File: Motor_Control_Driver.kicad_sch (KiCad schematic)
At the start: 10 parts, among them IC1002 DRV8214RTER

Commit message: Added footprints, images, almost finished all èages except for the MCU
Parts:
- R1002: renamed from R621; footprint (none) -> Resistor_SMD:R_0402_1005Metric; Manufacturer (none) -> KOA Speer; Manufacturer Part Number (none) -> RK73H1ETTP3300F; Supplier (none) -> Mouser Electronics; Supplier Part Number (none) -> 660-RK73H1ETTP3300F
- renumbered C622 to C1001, C620 to C1002, C624 to C1003, IC1002 to IC1001, LED502 to LED1001, R619 to R1001, R623 to R1003, TP602 to TP1001, TP604 to TP1002
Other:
- note added: "WQFN-16 3x3 mm"

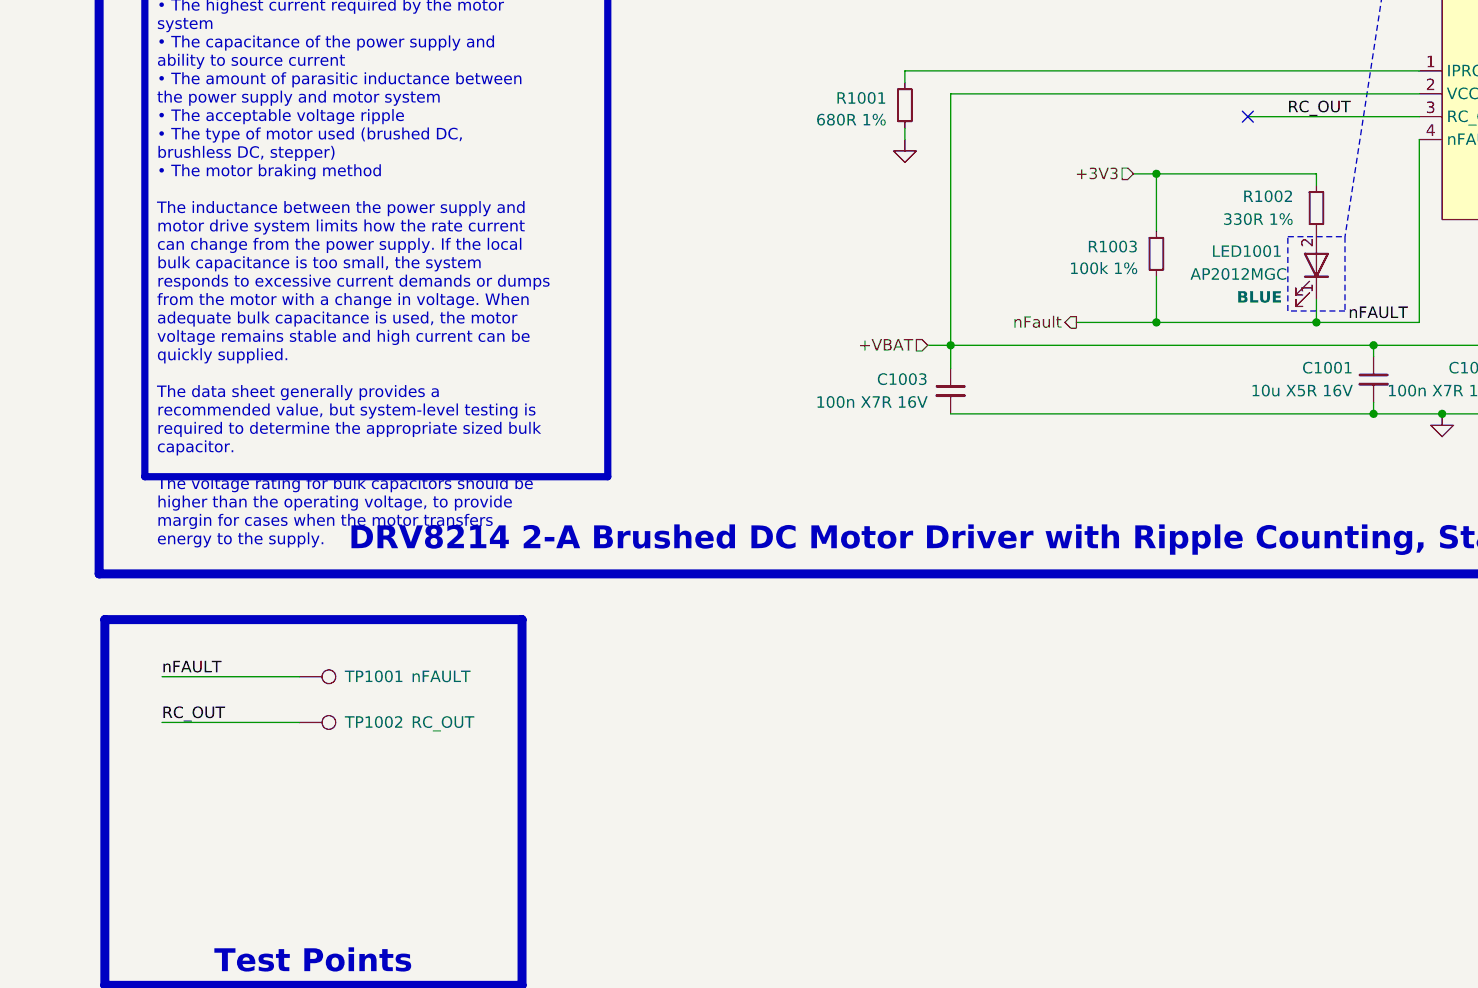
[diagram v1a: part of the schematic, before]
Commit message: Added RGB LED, added motor connectors, added test points, imported all 3D models
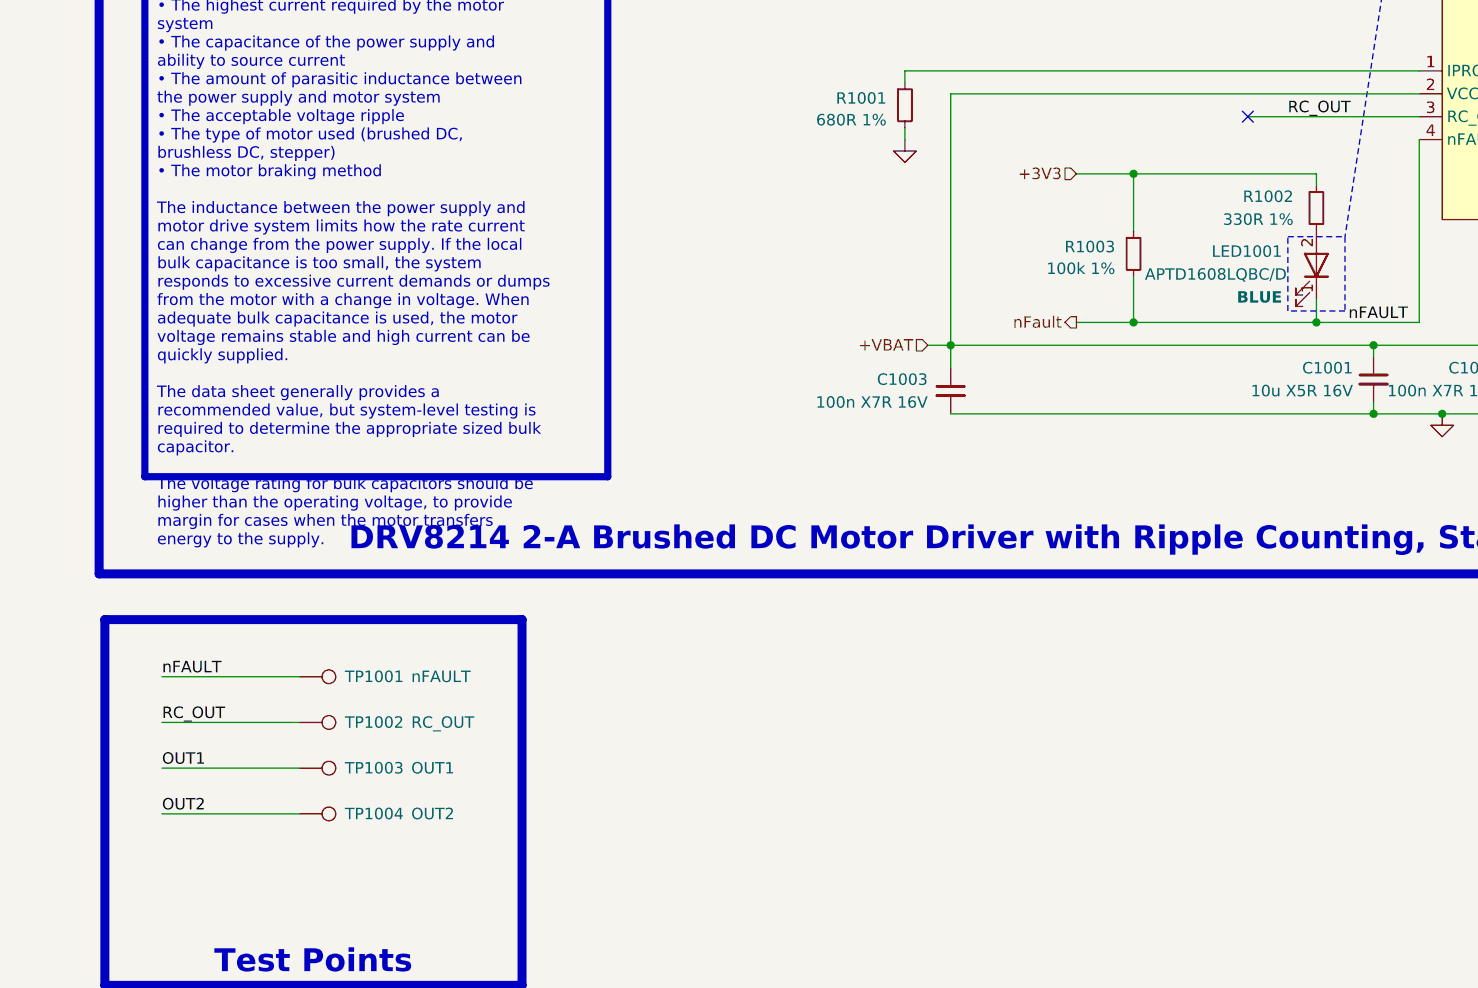
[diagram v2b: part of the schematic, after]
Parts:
- added TP1003: OUT1, 0_Plume:TestPoint_Pad_D0.5mm_Back, symbol Connector:TestPoint
- added TP1004: OUT2, 0_Plume:TestPoint_Pad_D0.5mm_Back, symbol Connector:TestPoint
- IC1001: footprint Package_DFN_QFN:WQFN-16-1EP_3x3mm_P0.5mm_EP1.68x1.68mm_ThermalVias -> 0_Plume:WQFN-16-1EP_3x3mm_P0.5mm_EP1.68x1.68mm_ThermalVias; Manufacturer (none) -> Texas Instruments; Manufacturer Part Number (none) -> DRV8214RTER; Supplier (none) -> Mouser Electronics; Supplier Part Number (none) -> 595-DRV8214RTER
- LED1001: footprint Charge_Manager_FP:KingBright_LED_0805 -> 0_Plume:KingBright_LED_0603; Manufacturer Part Number AP2012MGC -> APTD1608LQBC/D; Supplier Part Number 604-AP2012MGC -> 604-APTD1608LQBCD
- TP1001, TP1002: footprint 0_Zenith:TestPoint_Pad_D0.5mm_Front -> 0_Plume:TestPoint_Pad_D0.5mm_Back
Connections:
- net OUT1: now also TP1003.1
- net OUT2: now also TP1004.1
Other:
- moved on the sheet: R1003

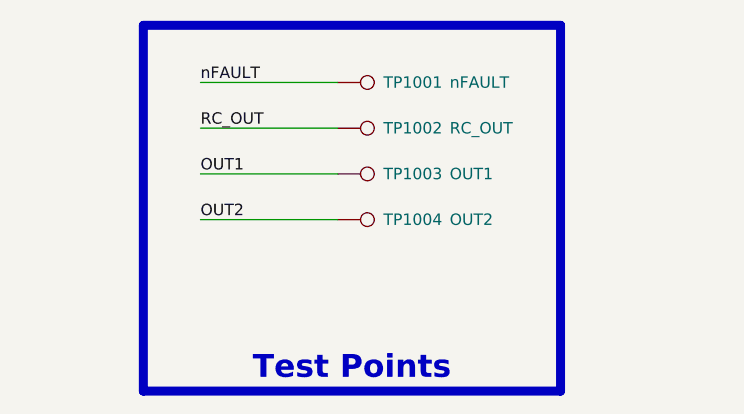
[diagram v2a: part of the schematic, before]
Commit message: Finished schematic, imported all footprints, all 3D models and created STM32 project, now need to proofread shematic before layout
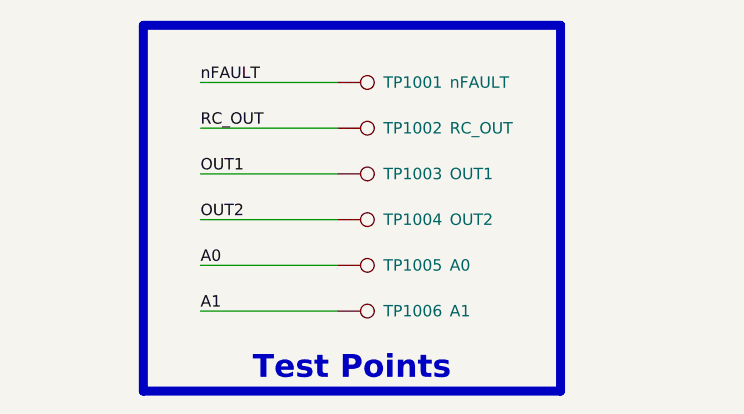
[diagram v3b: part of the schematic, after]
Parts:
- added TP1005: A0, 0_Plume:TestPoint_Pad_D0.5mm_Back, symbol Connector:TestPoint
- added TP1006: A1, 0_Plume:TestPoint_Pad_D0.5mm_Back, symbol Connector:TestPoint
- R1001: Manufacturer Panasonic -> (none); Manufacturer Part Number ERJ-2RKF1003X -> (none); Supplier Part Number 667-ERJ-2RKF1003X -> (none)
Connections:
- net A0: now also TP1005.1
- net A1: now also TP1006.1

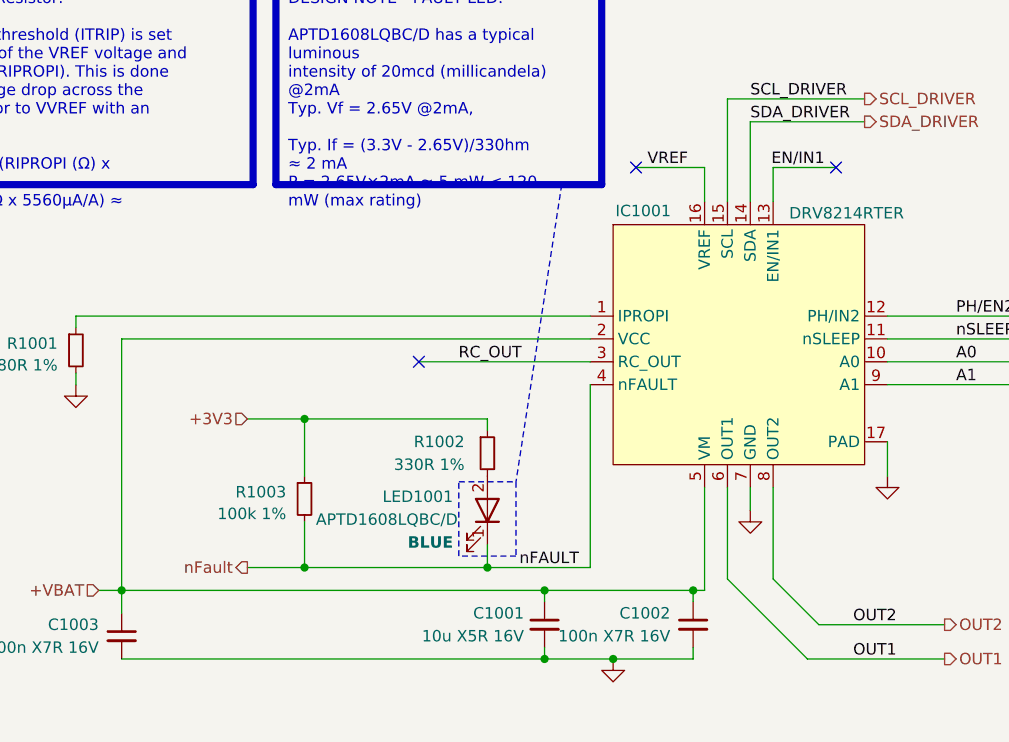
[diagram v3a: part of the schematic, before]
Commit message: Reviewed shematic, cleaned all DRC errors, chosed stackup, started layout
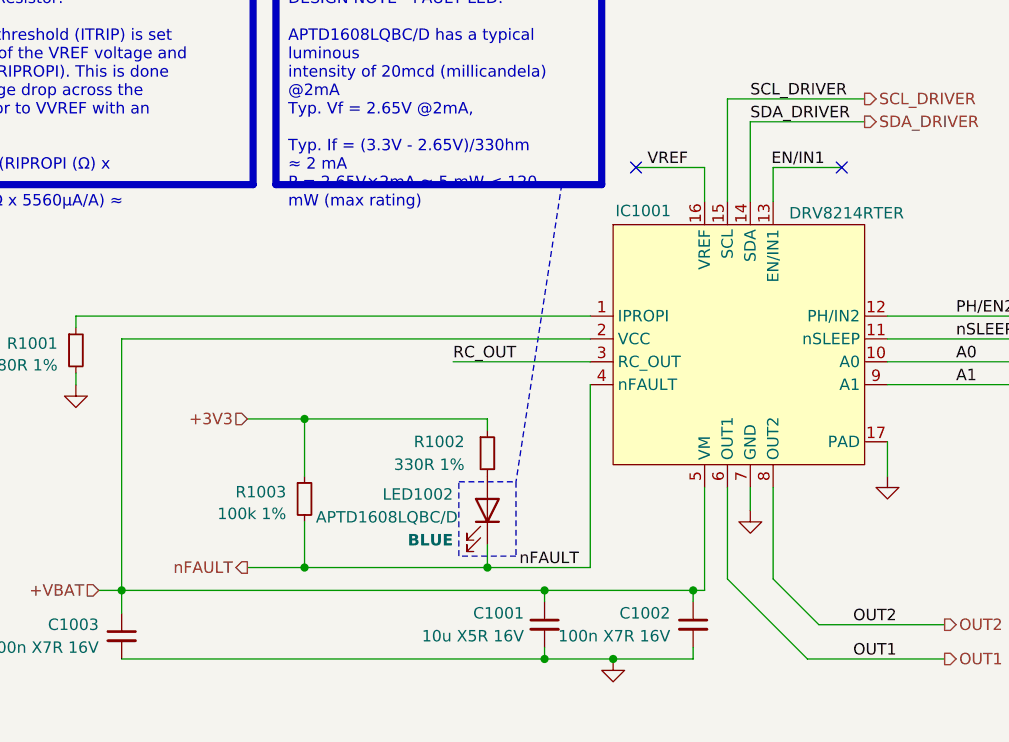
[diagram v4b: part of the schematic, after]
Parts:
- removed LED1001: BLUE, 0_Plume:KingBright_LED_0603, symbol Charge_Manager_SYM:SM1206SRC
- added LED1002: BLUE, 0_Plume:KingBright_LED_0603, symbol Device:LED
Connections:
- net at R1002.2: now also LED1002.2 (A)
- net nFault renamed nFAULT
- net nFAULT: now also LED1002.1 (K)
- no-connect marks 4 -> 3

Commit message: Cleaned repo, cleaned and exported shematic, advanced rough layout
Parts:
- renumbered LED1002 to LED1001
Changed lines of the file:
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@@
 	(title_block
 		(title "Motor Control - Driver ")
-		(date "2025-02-16")
+		(date "2025-04-05")
 		(rev "${REVISION}")
 	)
@@
 			"ZAAAAHAAAABjAAAALwAAAGoAAAB2AAAARwAAAEQAAABjAAAASgAAAHQAAABJAAAANgAAAGYAAAB1"
 			"AAAAVAAAADcAAABqAAAAdwAAADQAAAB3AAAARgAAAGUAAABEAAAARAAAAG0AAABtAAAAQgAAADAA"
-			"AABNAAAAbAAAAHIAAA=="
+			"AABNAAAAbAAAAHIAAAA1AAAASgAAAFAAAAB3AAAAaAAAAHYAAAAvAAAAYgAAAEsAAAAwAAAAMAAA"
+			"AGMAAAA2AAAAVQAAAEQAAAB1AAAAdgAAADYAAABFAAAAZgAAADMAAAB0AAAAVwAAAGMAAABZAAAA"
+			"dQAAAGYAAABPAAAASQAAAE4AAABEAAAAdgAAAEoAAAAxAAAAYgAAADgAAABhAAAAUQAAADkAAABN"
+			"AAAALwAAAGgAAABhAAAAZgAAAFEAAABTAAAAWAAAAGUAAABhAAAAUAAAAHIAAABNAAAANwAAADYA"
+			"AABrAAAAQwAAAHMAAABKAAAAeQAAAHYAAABSAAAAdgAAACsAAABoAAAARQAAAFAAAABhAAAAYwAA"
+			"AFkAAABuAAAAcAAAAE8AAAAvAAAAaAAAAEYAAAA2AAAAMwAAAHcAAAA0AAAANAAAAC8AAABkAAAA"
+			"KwAAAHgAAAA1AAAAKwAAAEgAAAArAAAAMAAAAHoAAABYAAAAWgAAAG4AAAArAAAAawAAAEwAAABT"
+			"AAAAVQAAAEkAAABUAAAALwAAADQAAABTAAAAMAAAAGQAAABzAAAAQgAAAG8AAAAxAAAAcwAAAFIA"
+			"AAA4AAAASQAAAFgAAABjAAAAUAAAADMAAAAwAAAARwAAAG8AAABPAAAAVgAAADYAAABVAAAATwAA"
+			"AFgAAAB6AAAAWQAAAC8AAABVAAAAQgAAADMAAABsAAAANAAAAHEAAABFAAAAMwAAAGgAAAAyAAAA"
+			"KwAAACsAAAAyAAAANgAAAGMAAABDAAAAdQAAAEQAAAA3AAAARAAAAFIAAABvAAAAOAAAADkAAAB4"
+			"AAAAcgAAADQAAABuAAAAVAAAAHoAAABRAAAANwAAADEAAAA3AAAAWAAAAGUAAABpAAAAQgAAAHcA"
+			"AABrAAAAeQAAAHMAAAA4AAAAKwAAADYAAAAzAAAAVQAAAFcAAAArAAAAUAAAAGMAAABDAAAAVQAA"
+			"AG0AAABKAAAATQAAAGcAAABJAAAAMQAAAE0AAABIAAAAVwAAAGEAAABIAAAAWAAAAHoAAABPAAAA"
+			"SwAAAGUAAABvAAAAUQAAAE8AAABQAAAALwAAAGoAAABZAAAANwAAAEIAAABIAAAAYgAAAEsAAAB0"
+			"AAAAYwAAAHIAAAArAAAAdgAAADcAAAAwAAAARQAAADkAAABoAAAATAAAAFkAAABTAAAAMgAAAEEA"
+			"AAB2AAAAZwAAAGIAAAAwAAAARQAAAGYAAABuAAAAQQAAAEoAAABmAAAASwAAADkAAABFAAAAMgAA"
+			"AFEAAAByAAAAdQAAAE8AAABCAAAAUQAAAEMAAABaAAAAMwAAAHYAAABpAAAARwAAAEEAAAArAAAA"
+			"TgAAADcAAAAyAAAAdQAAAFEAAAA1AAAAKwAAAFIAAAB3AAAAUgAAAGcAAABRAAAARAAAAEIAAAB1"
+			"AAAAQQAAAEoAAAA3AAAATQAAAGIAAABKAAAANQAAAGUAAAB6AAAAYwAAAHYAAABYAAAATgAAAC8A"
+			"AAA5AAAAMQAAAGkAAABDAAAAWAAAADAAAAArAAAALwAAADEAAABFAAAAdgAAAE4AAAB6AAAATgAA"
+			"AFIAAABJAAAAUQAAAEoAAABuAAAAQgAAAFgAAAB1AAAAQgAAAHoAAABtAAAATAAAAGMAAAAxAAAA"
+			"cQAAAGMAAAArAAAANQAAADQAAABBAAAAeAAAAHcAAABqAAAAcwAAAHkAAABDAAAAOAAAAEEAAABa"
+			"AAAATQAAAEEAAAAzAAAAZQAAAGQAAABtAAAAZAAAAHcAAAAzAAAAKwAAAEsAAAByAAAAVAAAAEEA"
+			"AABBAAAARgAAAE8AAAB6AAAAawAAAG0AAAB1AAAAUwAAAGUAAABaAAAAdwAAAGQAAABKAAAAUgAA"
+			"AFYAAABIAAAAOAAAADAAAABTAAAAQwAAAEIAAAB3AAAAegAAAFQAAABzAAAATQAAADQAAABXAAAA"
+			"UgAAAE0AAABBAAAAegAAADAAAAB3AAAAegAAAE0AAAAxAAAALwAAAFEAAABQAAAATQAAAHUAAAB3"
+			"AAAATAAAAE8AAAB0AAAARQAAAEUAAAAxAAAAcgAAADYAAAB4AAAARwAAAHoAAAB0AAAAZAAAAFEA"
+			"AABSAAAAdQAAAGcAAABoAAAAWgAAAE8AAABwAAAAVQAAAEMAAABnAAAAVAAAADgAAABXAAAAUwAA"
+			"ADIAAABLAAAAcgAAAFQAAABrAAAAdAAAAC8AAAA0AAAAaAAAADkAAABjAAAAcwAAAGoAAABRAAAA"
+			"bAAAAGsAAAA0AAAAeAAAAFMAAABHAAAAcAAAAGkAAABDAAAATgAAAEMAAAA1AAAAKwAAAFoAAABN"
+			"AAAAMwAAAGkAAABQAAAAVQAAADgAAABGAAAAUgAAAGsAAABPAAAAVAAAAEMAAABuAAAANQAAAGMA"
+			"AABmAAAAaAAAAEwAAABCAAAAeAAAADkAAABKAAAASwAAAFUAAABlAAAASgAAAEEAAABvAAAAQwAA"
+			"ADEAAAArAAAASgAAAGoAAABzAAAAdAAAAHIAAABDAAAARwAAAHQAAAB3AAAAUgAAAEoAAABiAAAA"
+			"bgAAAGcAAAB2AAAALwAAAHgAAAB6AAAASQAAAHgAAAA1AAAALwAAAGEAAABjAAAALwAAADIAAAAv"
+			"AAAAMAAAADQAAABiAAAAOQAAAFQAAAA4AAAAWAAAAC8AAAA3AAAAagAAAC8AAAA4AAAANAAAAEQA"
+			"AAB6AAAAaAAAAHYAAA=="
 		)
 	)
@@
 		(on_board yes)
 		(dnp no)
-		(property "Reference" "LED1002"
+		(property "Reference" "LED1001"
 			(at 156.21 106.172 90)
 			(effects
@@
 			(project "Plume"
 				(path "/0650c7a8-acba-429c-9f8e-eec0baf0bc1c/fede4c36-00cc-4d3d-b71c-5243ba232202/1d734d3e-47bf-494d-ad56-d8a87b193fe6/1bef5081-0788-4eb3-836e-648a382f2b6c"
-					(reference "LED1016")
+					(reference "LED2401")
 					(unit 1)
 				)
 				(path "/0650c7a8-acba-429c-9f8e-eec0baf0bc1c/fede4c36-00cc-4d3d-b71c-5243ba232202/1d734d3e-47bf-494d-ad56-d8a87b193fe6/1e0adc35-acd6-45f6-ade3-19c3ded56ec5"
-					(reference "LED1014")
+					(reference "LED2201")
 					(unit 1)
 				)
 				(path "/0650c7a8-acba-429c-9f8e-eec0baf0bc1c/fede4c36-00cc-4d3d-b71c-5243ba232202/1d734d3e-47bf-494d-ad56-d8a87b193fe6/2c88a68a-6853-461c-81b1-6f7689a27c20"
-					(reference "LED1018")
+					(reference "LED2601")
 					(unit 1)
 				)
 				(path "/0650c7a8-acba-429c-9f8e-eec0baf0bc1c/fede4c36-00cc-4d3d-b71c-5243ba232202/1d734d3e-47bf-494d-ad56-d8a87b193fe6/4b6057ab-9569-4a50-b2ec-0116f8746044"
-					(reference "LED1002")
+					(reference "LED1001")
 					(unit 1)
 				)
 				(path "/0650c7a8-acba-429c-9f8e-eec0baf0bc1c/fede4c36-00cc-4d3d-b71c-5243ba232202/1d734d3e-47bf-494d-ad56-d8a87b193fe6/565b7884-038c-44a1-b912-b549fc8fe526"
-					(reference "LED1019")
+					(reference "LED2701")
 					(unit 1)
 				)
 				(path "/0650c7a8-acba-429c-9f8e-eec0baf0bc1c/fede4c36-00cc-4d3d-b71c-5243ba232202/1d734d3e-47bf-494d-ad56-d8a87b193fe6/618a934c-f37a-4b6b-a940-4c63d3ecf5b8"
-					(reference "LED1004")
+					(reference "LED1201")
 					(unit 1)
 				)
 				(path "/0650c7a8-acba-429c-9f8e-eec0baf0bc1c/fede4c36-00cc-4d3d-b71c-5243ba232202/1d734d3e-47bf-494d-ad56-d8a87b193fe6/6fd40467-a198-41ea-a4d9-2f02150cb069"
-					(reference "LED1012")
+					(reference "LED2001")
 					(unit 1)
 				)
 				(path "/0650c7a8-acba-429c-9f8e-eec0baf0bc1c/fede4c36-00cc-4d3d-b71c-5243ba232202/1d734d3e-47bf-494d-ad56-d8a87b193fe6/77903578-77ce-4db2-abc4-7e1e598c1c81"
-					(reference "LED1006")
+					(reference "LED1401")
 					(unit 1)
 				)
 				(path "/0650c7a8-acba-429c-9f8e-eec0baf0bc1c/fede4c36-00cc-4d3d-b71c-5243ba232202/1d734d3e-47bf-494d-ad56-d8a87b193fe6/7c61966c-565f-49d7-b6ca-f610dc5c20c4"
-					(reference "LED1009")
+					(reference "LED1701")
 					(unit 1)
 				)
 				(path "/0650c7a8-acba-429c-9f8e-eec0baf0bc1c/fede4c36-00cc-4d3d-b71c-5243ba232202/1d734d3e-47bf-494d-ad56-d8a87b193fe6/81e8f56c-af65-4f8a-ac2a-2a96e060003e"
-					(reference "LED1017")
+					(reference "LED2501")
 					(unit 1)
 				)
 				(path "/0650c7a8-acba-429c-9f8e-eec0baf0bc1c/fede4c36-00cc-4d3d-b71c-5243ba232202/1d734d3e-47bf-494d-ad56-d8a87b193fe6/837d1b79-0cf8-47d2-94c8-ae5e6673543f"
-					(reference "LED1007")
+					(reference "LED1501")
 					(unit 1)
 				)
 				(path "/0650c7a8-acba-429c-9f8e-eec0baf0bc1c/fede4c36-00cc-4d3d-b71c-5243ba232202/1d734d3e-47bf-494d-ad56-d8a87b193fe6/a59cea44-0368-4827-8b20-bd6f6290079f"
-					(reference "LED1010")
+					(reference "LED1801")
 					(unit 1)
 				)
 				(path "/0650c7a8-acba-429c-9f8e-eec0baf0bc1c/fede4c36-00cc-4d3d-b71c-5243ba232202/1d734d3e-47bf-494d-ad56-d8a87b193fe6/b00e0a5c-3b4e-4893-8d8f-45d2476d3944"
-					(reference "LED1015")
+					(reference "LED2301")
 					(unit 1)
 				)
 				(path "/0650c7a8-acba-429c-9f8e-eec0baf0bc1c/fede4c36-00cc-4d3d-b71c-5243ba232202/1d734d3e-47bf-494d-ad56-d8a87b193fe6/b2f0397c-abd1-4c1a-916c-d70b6c0cff56"
-					(reference "LED1011")
+					(reference "LED1901")
 					(unit 1)
 				)
 				(path "/0650c7a8-acba-429c-9f8e-eec0baf0bc1c/fede4c36-00cc-4d3d-b71c-5243ba232202/1d734d3e-47bf-494d-ad56-d8a87b193fe6/b8854900-2c64-495d-9ce8-dbffd3c5e680"
-					(reference "LED1013")
+					(reference "LED2101")
 					(unit 1)
 				)
 				(path "/0650c7a8-acba-429c-9f8e-eec0baf0bc1c/fede4c36-00cc-4d3d-b71c-5243ba232202/1d734d3e-47bf-494d-ad56-d8a87b193fe6/dc610de4-0abe-436a-8570-cee68e79b8b4"
-					(reference "LED1008")
+					(reference "LED1601")
 					(unit 1)
 				)
 				(path "/0650c7a8-acba-429c-9f8e-eec0baf0bc1c/fede4c36-00cc-4d3d-b71c-5243ba232202/1d734d3e-47bf-494d-ad56-d8a87b193fe6/e999b2a7-69dc-47d5-a1b1-2b1f8537e21f"
-					(reference "LED1005")
+					(reference "LED1301")
 					(unit 1)
 				)
 				(path "/0650c7a8-acba-429c-9f8e-eec0baf0bc1c/fede4c36-00cc-4d3d-b71c-5243ba232202/1d734d3e-47bf-494d-ad56-d8a87b193fe6/f9d6be9e-1658-4990-b3db-7b3ff351ff5f"
-					(reference "LED1003")
+					(reference "LED1101")
 					(unit 1)
 				)

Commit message: Advanced rough layout
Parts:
- C1002: value 100n X7R 16V -> 100n X7R 50V; footprint Capacitor_SMD:C_0402_1005Metric -> Capacitor_SMD:C_0603_1608Metric; Manufacturer Samsung Electro-Mechanics -> KEMET; Manufacturer Part Number CL05B104KO5VPNC -> C0603C104J5RACAUTO; Supplier Part Number 187-CL05B104KO5VPNC -> 80-C0603C104J5RAUTO
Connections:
- net FAULT_LED: now reaches LED1001.2 (A), R1002.2
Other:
- moved on the sheet: R1002
